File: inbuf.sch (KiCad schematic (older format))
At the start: 11 parts

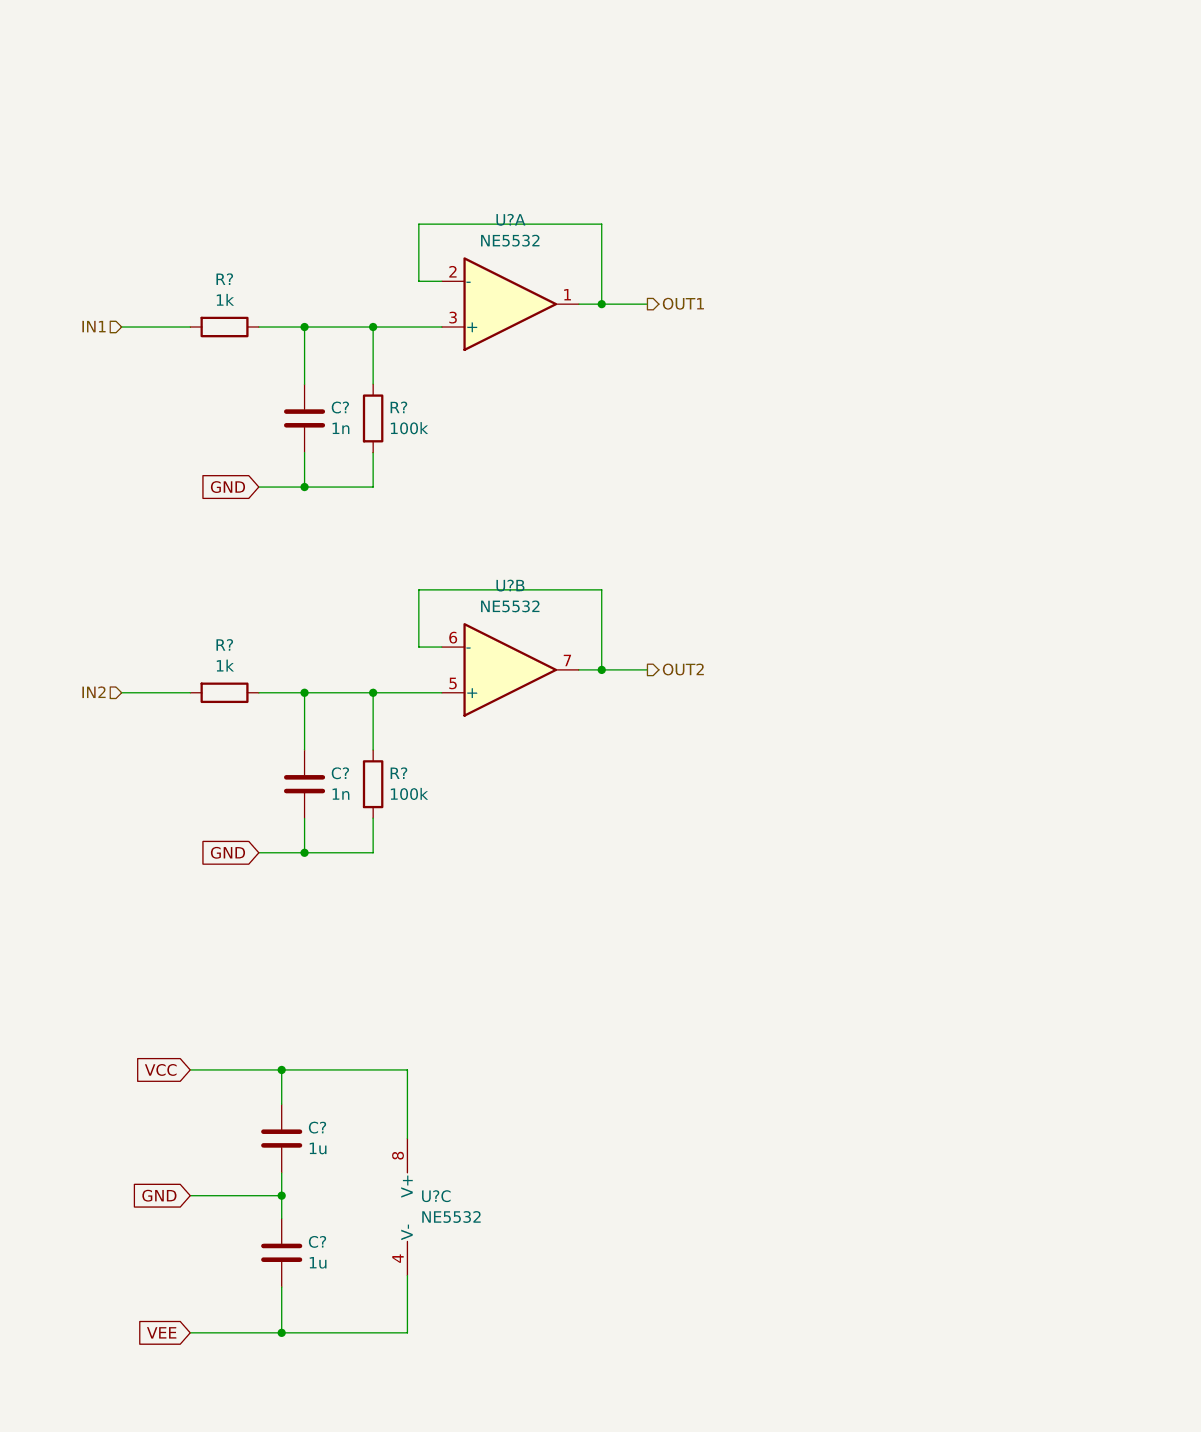
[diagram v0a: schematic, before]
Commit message: improved PSU, gain up front, reordered filter stages, shrunk rumble filter
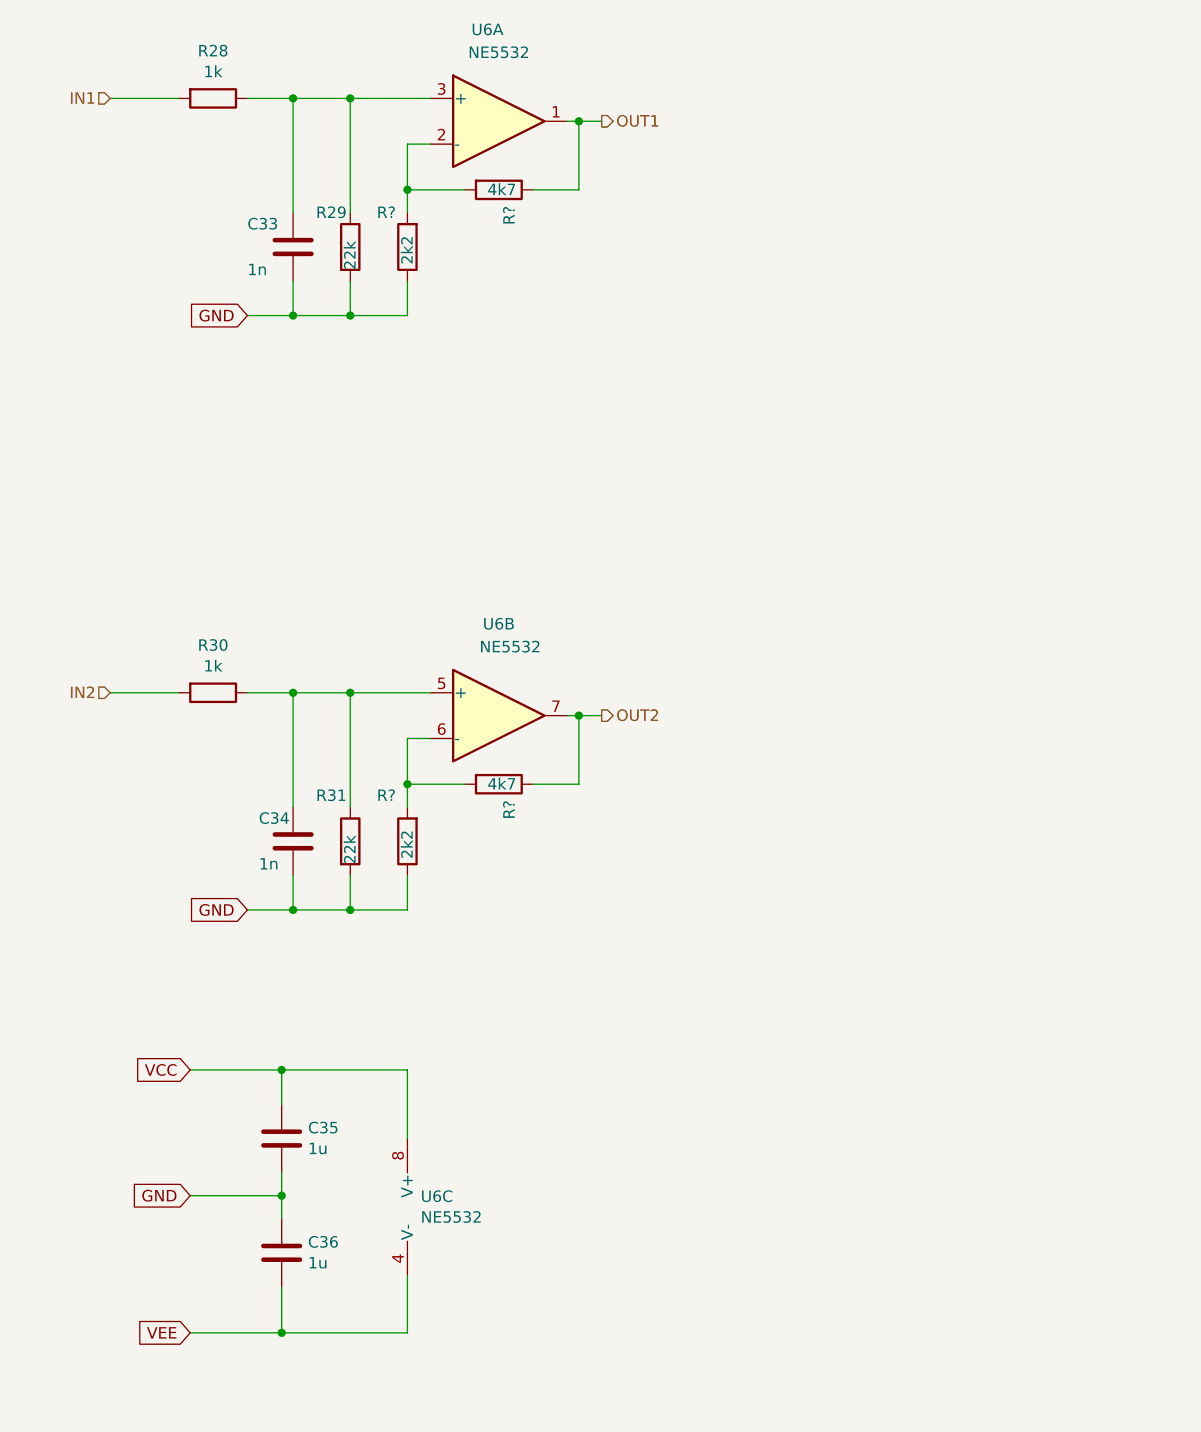
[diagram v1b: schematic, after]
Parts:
- added R? (x2): 4k7, Resistors_SMD:R_0805, symbol Device:R
- added R? (x2): 2k2, Resistors_SMD:R_0805, symbol Device:R
- R29, R31: renamed from R?; value 100k -> 22k
- U6: renamed from U?; footprint (none) -> Housings_DIP:DIP-8_W7.62mm_Socket
- gave numbers to parts that had none: 6
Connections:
- net GND: now also R?.1, R?.1
- net OUT1: now also R?.1; no longer U6.2 (-)
- net OUT2: now also R?.1; no longer U6.6 (-)
- new net: R?.2, R?.2, U6.2 (-)
- new net: R?.2, R?.2, U6.6 (-)
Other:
- moved on the sheet: C33, C34, R28, R29, R30, R31, U6A, U6B

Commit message: added buffered volume pot, and fixed subsonic filter added signal taps for external transforms/filters to be added later
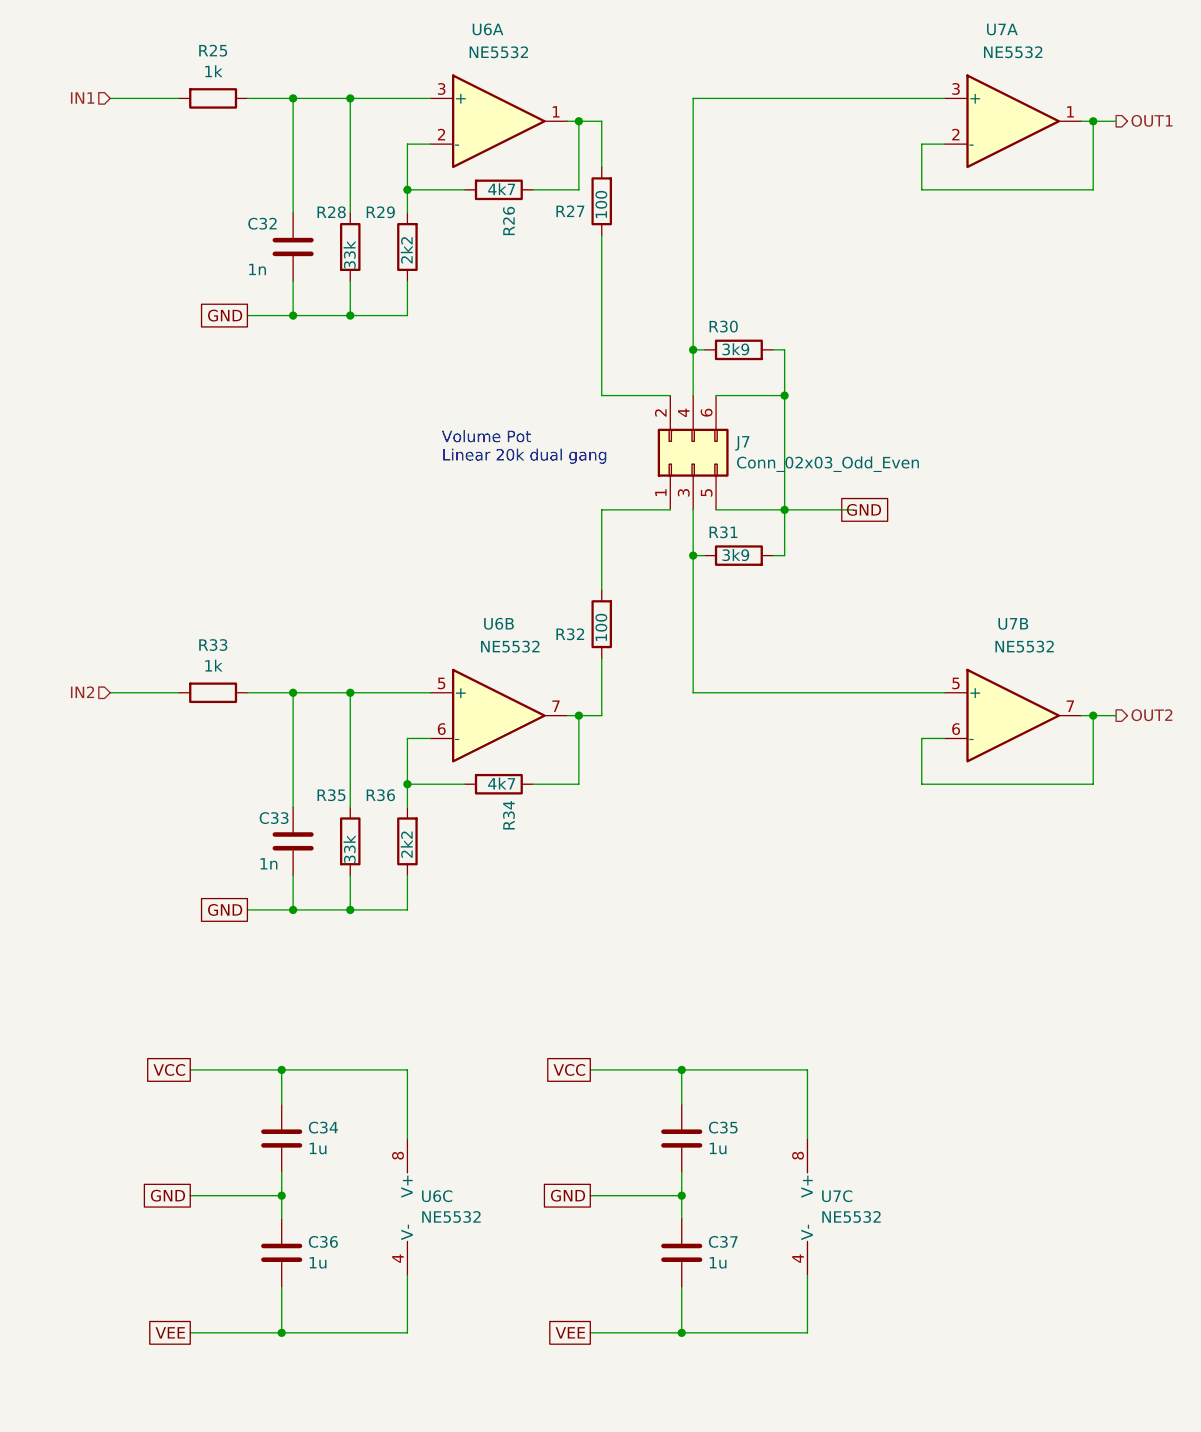
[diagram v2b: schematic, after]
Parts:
- added C35, C37: 1u, Capacitors_SMD:C_0805, symbol Device:C
- added J7: Conn_02x03_Odd_Even, Pin_Headers:Pin_Header_Straight_2x03_Pitch2.54mm, symbol Connector_Generic:Conn_02x03_Odd_Even
- added R27, R32: 100, Resistors_SMD:R_0805, symbol Device:R
- added R30, R31: 3k9, Resistors_SMD:R_0805, symbol Device:R
- added U7: NE5532, Housings_DIP:DIP-8_W7.62mm_Socket, symbol Amplifier_Operational:NE5532
- R28: renamed from R29; value 22k -> 33k
- R35: renamed from R31; value 22k -> 33k
- gave numbers to parts that had none: 4
- renumbered C33 to C32, C34 to C33, C35 to C34, R28 to R25, R30 to R33
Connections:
- net GND: now also C35.2, C37.1, J7.5 (Pin_5), J7.6 (Pin_6), R30.2, R31.2
- net OUT1: now also U7.1, U7.2 (-); no longer R26.1, U6.1
- net OUT2: now also U7.6 (-), U7.7; no longer R34.1, U6.7
- net VCC: now also C35.1, U7.8 (V+)
- net VEE: now also C37.2, U7.4 (V-)
- new net: R26.1, R27.2, U6.1
- new net: R32.1, R34.1, U6.7
- new net: J7.3 (Pin_3), R31.1, U7.5 (+)
- new net: J7.4 (Pin_4), R30.1, U7.3 (+)
- new net: J7.1 (Pin_1), R32.2
- new net: J7.2 (Pin_2), R27.1
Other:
- note added: "Volume Pot\nLinear 20k dual gang"

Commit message: inverted LF processing chain, now with BW2 subsonic filter
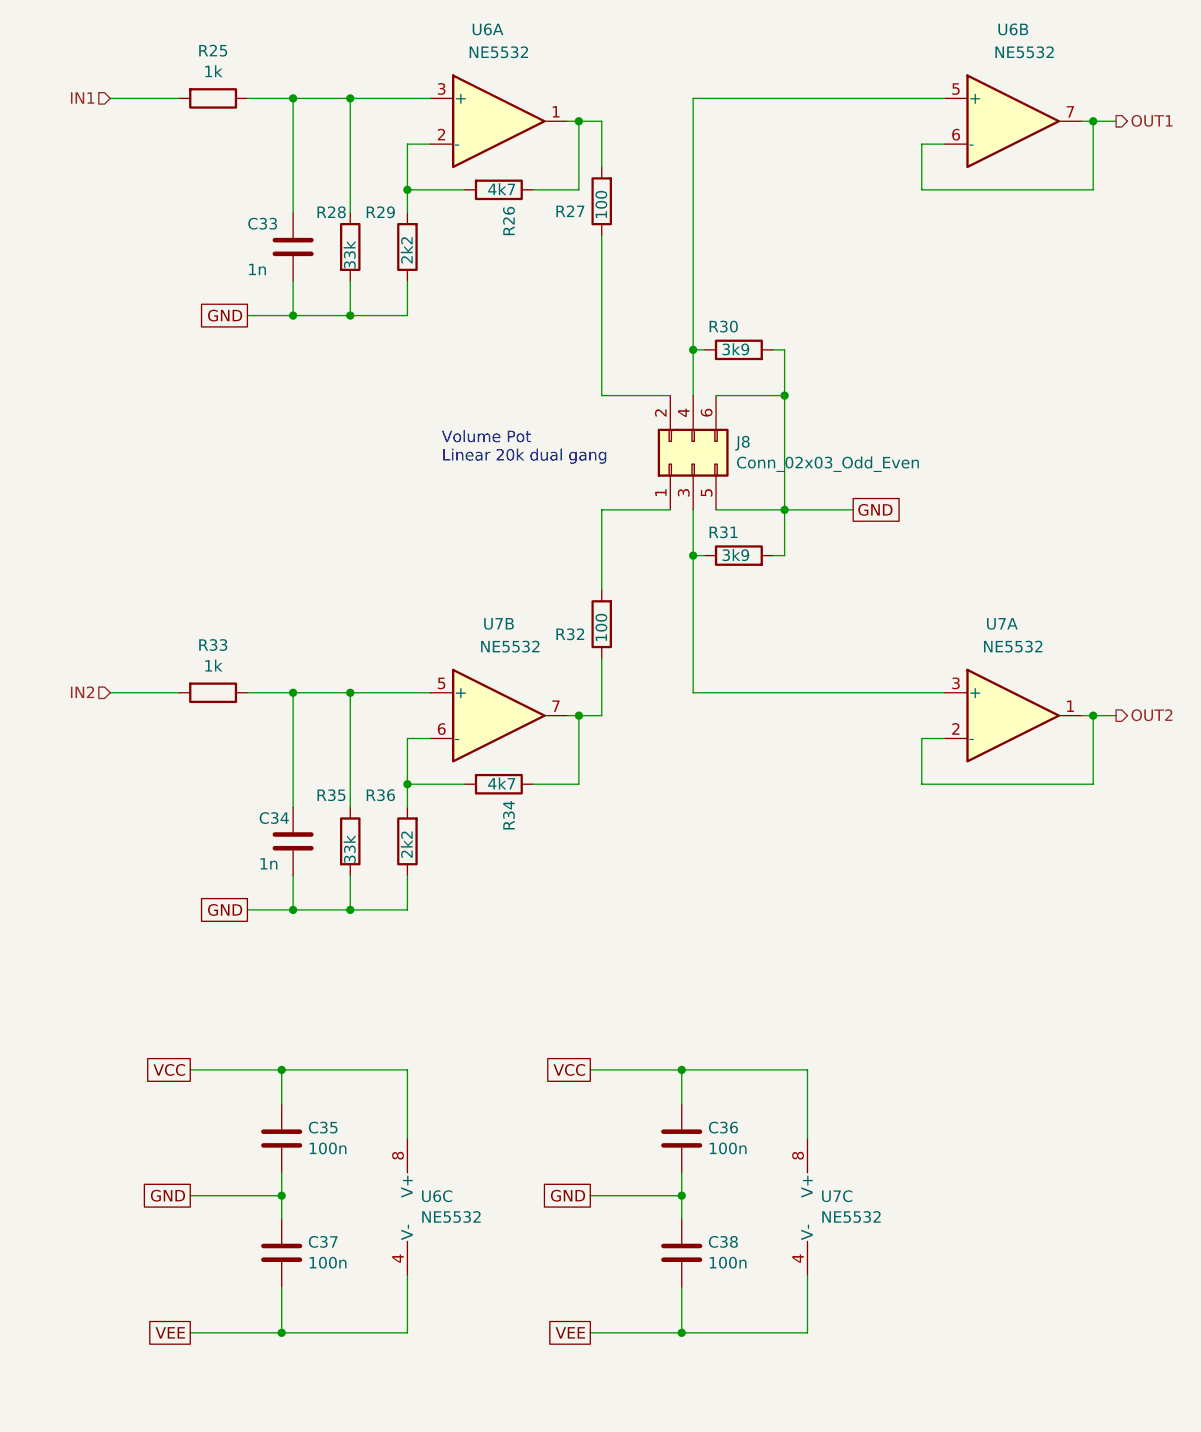
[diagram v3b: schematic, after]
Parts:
- C35: renamed from C34; value 1u -> 100n
- C36: renamed from C35; value 1u -> 100n
- C37: renamed from C36; value 1u -> 100n
- C38: renamed from C37; value 1u -> 100n
- renumbered C32 to C33, C33 to C34, J7 to J8, U7 to U6, U6 to U7
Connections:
- net OUT1: now also U6.6 (-), U6.7; no longer U7.1, U7.2 (-)
- net OUT2: now also U7.1, U7.2 (-); no longer U6.6 (-), U6.7
- net at J8.3 (Pin_3), R31.1: now also U7.3 (+); no longer U6.5 (+)
- net at J8.4 (Pin_4), R30.1: now also U6.5 (+); no longer U7.3 (+)
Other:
- moved on the sheet: U6B, U7A
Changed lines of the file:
@@
 $Descr A4 11693 8268
 encoding utf-8
-Sheet 6 19
+Sheet 6 17
 Title "Input Buffers, 10dB Gain"
 Date "2021-10-03"
@@
 $EndDescr
 $Comp
-L Amplifier_Operational:NE5532 U6
+L Amplifier_Operational:NE5532 U7
 U 2 1 6159C1D0
 P 3700 4400
-F 0 "U6" H 3700 4800 50  0000 C CNN
+F 0 "U7" H 3700 4800 50  0000 C CNN
 F 1 "NE5532" H 3750 4700 50  0000 C CNN
 F 2 "Housings_DIP:DIP-8_W7.62mm_Socket" H 3700 4400 50  0001 C CNN
@@
 $EndComp
 $Comp
-L Device:C C32
+L Device:C C33
 U 1 1 615A3CF4
 P 2800 2350
-F 0 "C32" H 2600 2450 50  0000 L CNN
+F 0 "C33" H 2600 2450 50  0000 L CNN
 F 1 "1n" H 2600 2250 50  0000 L CNN
 F 2 "Capacitors_SMD:C_0805" H 2838 2200 50  0001 C CNN
@@
 AR Path="/61596D2A/615A8570" Ref="C?"  Part="1"
 AR Path="/61597701/615A8570" Ref="C?"  Part="1"
-AR Path="/6159A74A/615A8570" Ref="C36"  Part="1"
-F 0 "C36" H 2865 6796 50  0000 L CNN
-F 1 "1u" H 2865 6705 50  0000 L CNN
+AR Path="/6159A74A/615A8570" Ref="C37"  Part="1"
+F 0 "C37" H 2865 6796 50  0000 L CNN
+F 1 "100n" H 2865 6705 50  0000 L CNN
 F 2 "Capacitors_SMD:C_0805" H 2788 6600 50  0001 C CNN
 F 3 "~" H 2750 6750 50  0001 C CNN
@@
 AR Path="/61596D2A/615A8576" Ref="C?"  Part="1"
 AR Path="/61597701/615A8576" Ref="C?"  Part="1"
-AR Path="/6159A74A/615A8576" Ref="C34"  Part="1"
-F 0 "C34" H 2865 6296 50  0000 L CNN
-F 1 "1u" H 2865 6205 50  0000 L CNN
+AR Path="/6159A74A/615A8576" Ref="C35"  Part="1"
+F 0 "C35" H 2865 6296 50  0000 L CNN
+F 1 "100n" H 2865 6205 50  0000 L CNN
 F 2 "Capacitors_SMD:C_0805" H 2788 6100 50  0001 C CNN
 F 3 "~" H 2750 6250 50  0001 C CNN
@@
 	2800 5250 2800 5100
 $Comp
-L Device:C C33
+L Device:C C34
 U 1 1 615AEF58
 P 2800 4950
-F 0 "C33" H 2650 5050 50  0000 L CNN
+F 0 "C34" H 2650 5050 50  0000 L CNN
 F 1 "1n" H 2650 4850 50  0000 L CNN
 F 2 "Capacitors_SMD:C_0805" H 2838 4800 50  0001 C CNN
@@
 Wire Wire Line
 	3050 4300 3400 4300
-$Comp
-L Amplifier_Operational:NE5532 U7
-U 2 1 6190D927
-P 5950 4400
-F 0 "U7" H 5950 4800 50  0000 C CNN
-F 1 "NE5532" H 6000 4700 50  0000 C CNN
-F 2 "Housings_DIP:DIP-8_W7.62mm_Socket" H 5950 4400 50  0001 C CNN
-F 3 "http://www.ti.com/lit/ds/symlink/ne5532.pdf" H 5950 4400 50  0001 C CNN
-	2    5950 4400
-	1    0    0    -1
-$EndComp
 Text HLabel 6400 1800 2    50   Output ~ 0
 OUT1
 Text HLabel 6400 4400 2    50   Output ~ 0
 OUT2
-$Comp
-L Amplifier_Operational:NE5532 U7
-U 1 1 6190D92F
-P 5950 1800
-F 0 "U7" H 5900 2200 50  0000 C CNN
-F 1 "NE5532" H 5950 2100 50  0000 C CNN
-F 2 "Housings_DIP:DIP-8_W7.62mm_Socket" H 5950 1800 50  0001 C CNN
-F 3 "http://www.ti.com/lit/ds/symlink/ne5532.pdf" H 5950 1800 50  0001 C CNN
-	1    5950 1800
-	1    0    0    -1
-$EndComp
 Wire Wire Line
 	6250 1800 6300 1800
@@
 	5550 4500 5650 4500
 $Comp
-L Connector_Generic:Conn_02x03_Odd_Even J7
+L Connector_Generic:Conn_02x03_Odd_Even J8
 U 1 1 6191040E
 P 4550 3300
-F 0 "J7" V 4646 3112 50  0000 R CNN
+F 0 "J8" V 4646 3112 50  0000 R CNN
 F 1 "Conn_02x03_Odd_Even" V 4555 3112 50  0000 R CNN
 F 2 "Pin_Headers:Pin_Header_Straight_2x03_Pitch2.54mm" H 4550 3300 50  0001 C CNN
@@
 AR Path="/61596D2A/6198214A" Ref="C?"  Part="1"
 AR Path="/61597701/6198214A" Ref="C?"  Part="1"
-AR Path="/6159A74A/6198214A" Ref="C37"  Part="1"
-F 0 "C37" H 4615 6796 50  0000 L CNN
-F 1 "1u" H 4615 6705 50  0000 L CNN
+AR Path="/6159A74A/6198214A" Ref="C38"  Part="1"
+F 0 "C38" H 4615 6796 50  0000 L CNN
+F 1 "100n" H 4615 6705 50  0000 L CNN
 F 2 "Capacitors_SMD:C_0805" H 4538 6600 50  0001 C CNN
 F 3 "~" H 4500 6750 50  0001 C CNN
@@
 AR Path="/61596D2A/61982150" Ref="C?"  Part="1"
 AR Path="/61597701/61982150" Ref="C?"  Part="1"
-AR Path="/6159A74A/61982150" Ref="C35"  Part="1"
-F 0 "C35" H 4615 6296 50  0000 L CNN
-F 1 "1u" H 4615 6205 50  0000 L CNN
+AR Path="/6159A74A/61982150" Ref="C36"  Part="1"
+F 0 "C36" H 4615 6296 50  0000 L CNN
+F 1 "100n" H 4615 6205 50  0000 L CNN
 F 2 "Capacitors_SMD:C_0805" H 4538 6100 50  0001 C CNN
 F 3 "~" H 4500 6250 50  0001 C CNN
@@
 Wire Wire Line
 	5050 6850 5050 7100
-Text GLabel 5200 3500 2    50   UnSpc ~ 0
+Text GLabel 5250 3500 2    50   UnSpc ~ 0
 GND
 Wire Wire Line
@@
 Connection ~ 4950 3000
 Wire Wire Line
-	4550 1700 4550 2800
-Wire Wire Line
 	4550 2800 4600 2800
 Connection ~ 4550 2800
@@
 	4550 3700 4600 3700
 Connection ~ 4550 3700
+$Comp
+L Amplifier_Operational:NE5532 U7
+U 1 1 6190D92F
+P 5950 4400
+F 0 "U7" H 5900 4800 50  0000 C CNN
+F 1 "NE5532" H 5950 4700 50  0000 C CNN
+F 2 "Housings_DIP:DIP-8_W7.62mm_Socket" H 5950 4400 50  0001 C CNN
+F 3 "http://www.ti.com/lit/ds/symlink/ne5532.pdf" H 5950 4400 50  0001 C CNN
+	1    5950 4400
+	1    0    0    -1
+$EndComp
+$Comp
+L Amplifier_Operational:NE5532 U6
+U 2 1 6190D927
+P 5950 1800
+F 0 "U6" H 5950 2200 50  0000 C CNN
+F 1 "NE5532" H 6000 2100 50  0000 C CNN
+F 2 "Housings_DIP:DIP-8_W7.62mm_Socket" H 5950 1800 50  0001 C CNN
+F 3 "http://www.ti.com/lit/ds/symlink/ne5532.pdf" H 5950 1800 50  0001 C CNN
+	2    5950 1800
+	1    0    0    -1
+$EndComp
 Wire Wire Line
 	4550 3700 4550 4300
+Wire Wire Line
+	4550 1700 4550 2800
 $EndSCHEMATC
